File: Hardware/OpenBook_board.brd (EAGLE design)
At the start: 174.6 x 111.2 mm, 103 parts, among them IC1 BD5229G-TR, IC4 XC6220A331MR-G, J1 FH34SRJ-24S-0.5SH_99_, J2 SAMACSYS_PARTS_USB4110-GF-A, J3 QWIIC_RIGHT_ANGLE, J4 112A-TAAR-R03_ATTEND, Q1 20V/4.2A/52mΩ/1.4W, Q2 20V/4.2A/52mΩ/1.4W, Q3 SI1308EDL-T1-GE3, U1 W25Q512JVEIQ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

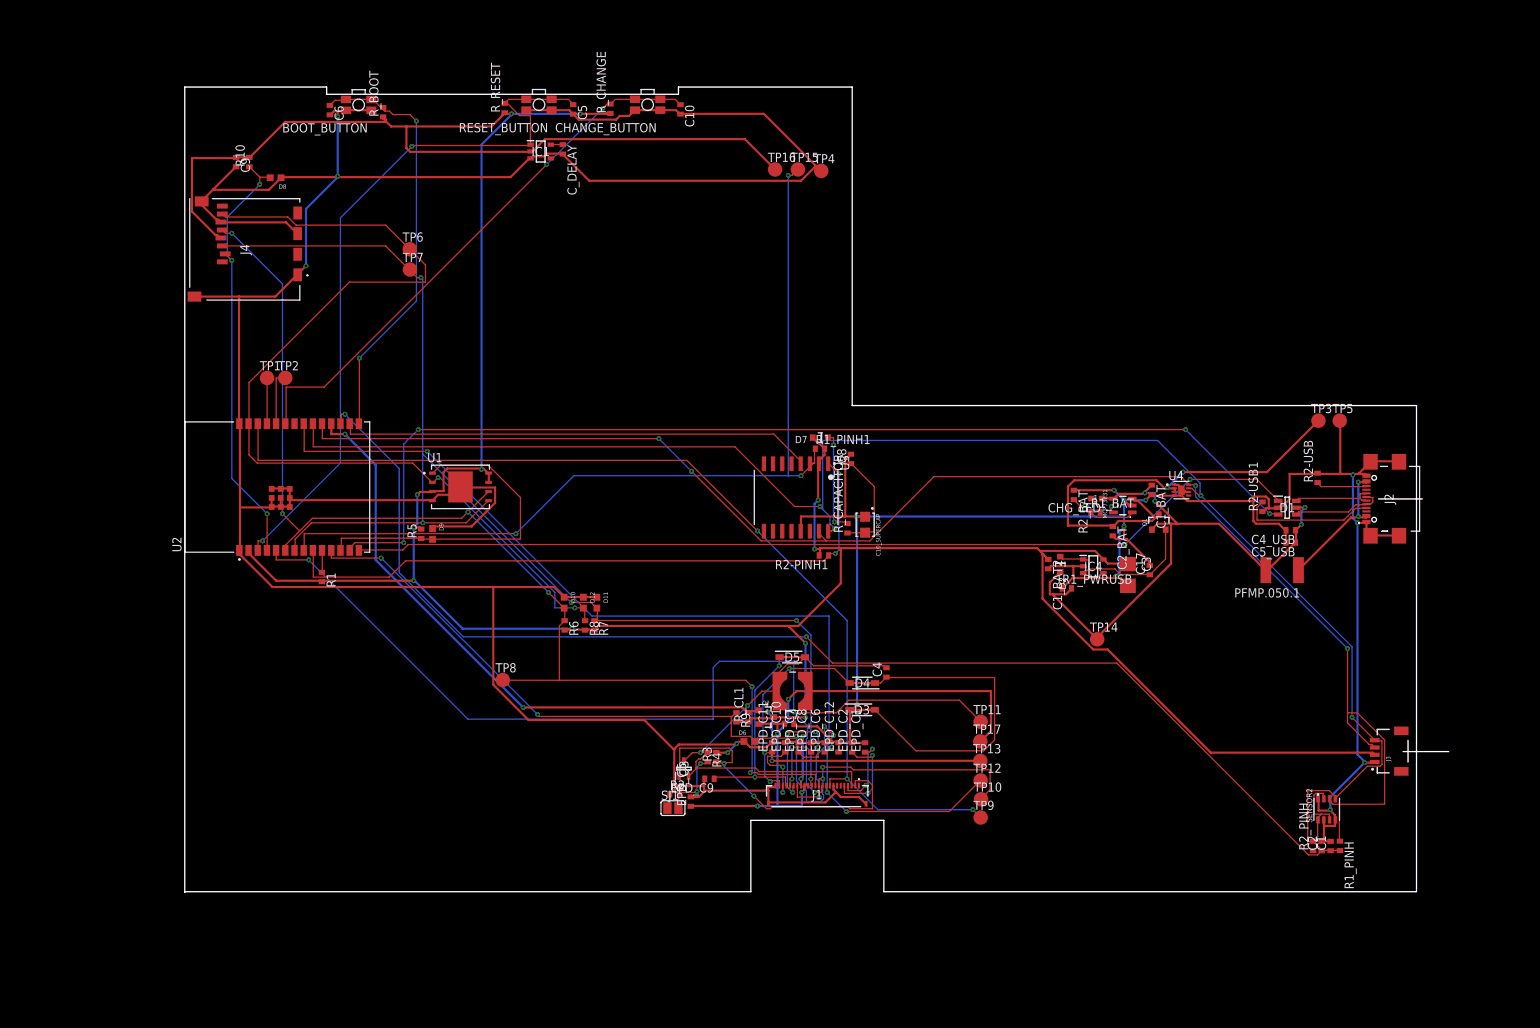
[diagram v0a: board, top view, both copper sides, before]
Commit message: Replaced board and schematic with the correct ones.
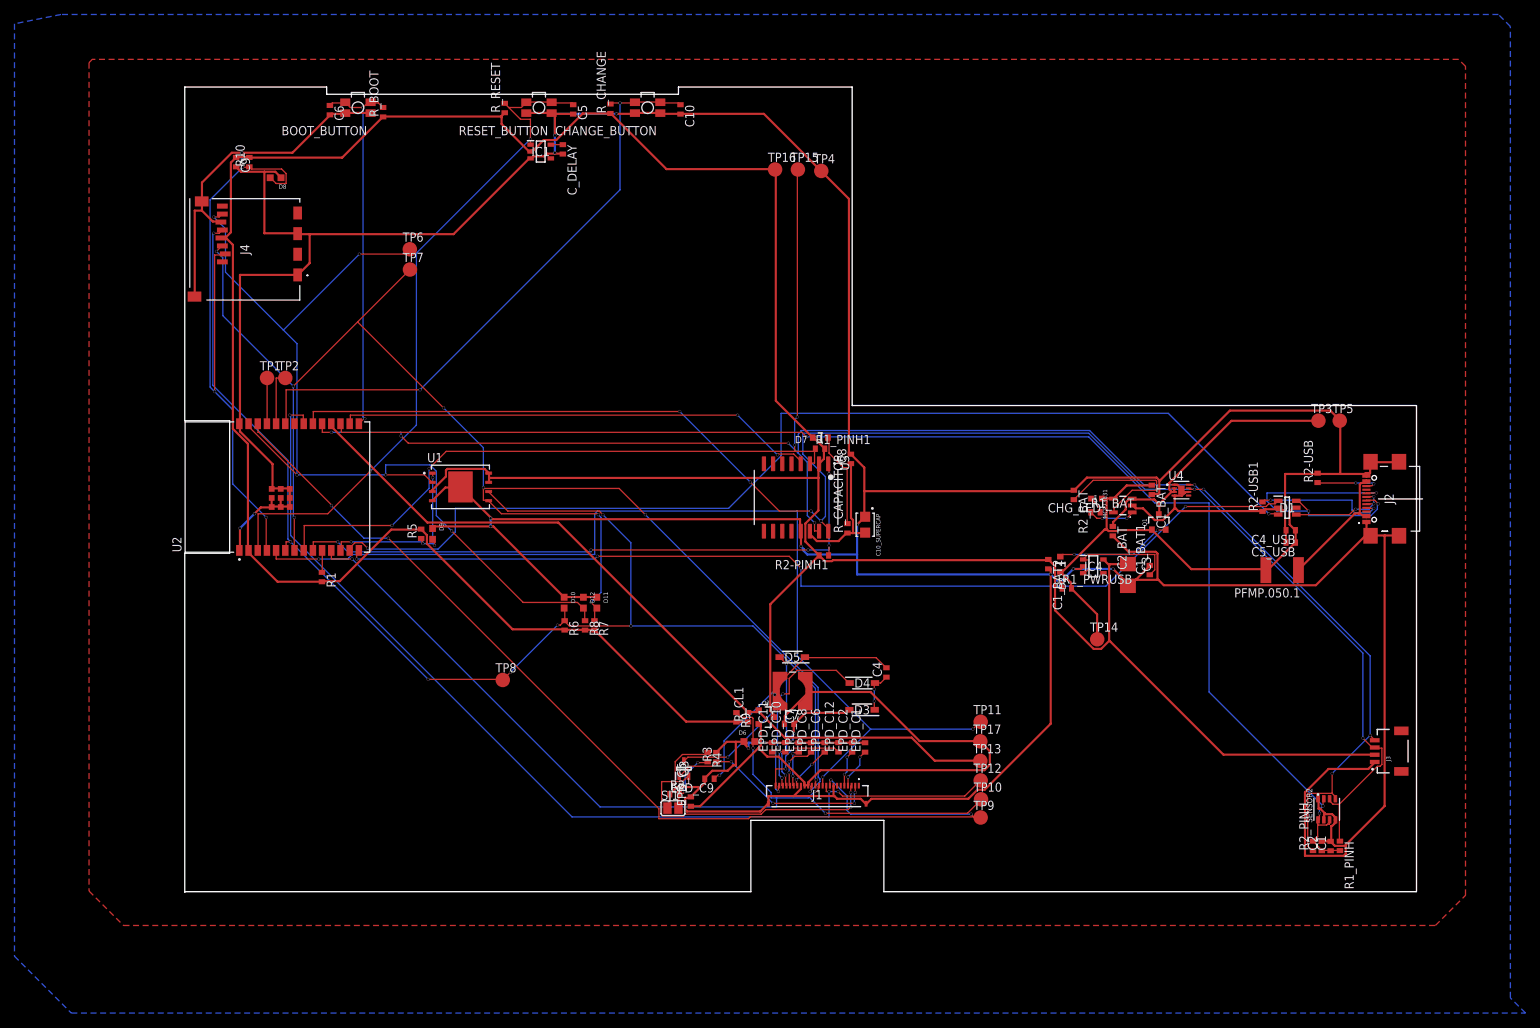
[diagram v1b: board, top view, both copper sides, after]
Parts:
- C1_BAT1, C5_USB: value (none) -> 4.7uF
- C4_USB: value (none) -> 100nF
- R1: value 2K -> 10K
- moved CHANGE_BUTTON 0.41 mm to (63.9, 108.3)
- moved RESET_BUTTON 0.41 mm to (48.9, 108.3)
- moved BOOT_BUTTON 0.40 mm to (23.9, 108.3)
- turned D3 to 180 degrees
- turned D4 to 0 degrees
- turned D5 to 180 degrees
- renumbered C17 to C1_BAT1
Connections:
- removed net N$17: C10_SUPERCAP.2, C8.1, R_CAPACITOR.1
- new net N$2: EPD_C12.1, J1.24
- net GND: no longer EPD_C12.1, J1.24
- net VRTC: now also C10_SUPERCAP.2, C8.1, R_CAPACITOR.1
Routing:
- net GND: track 760.1 -> 843.9 mm, vias 18 -> 19
- net N$7: track 52.0 -> 5.67 mm, vias 0 -> 2
- net SS_SD: track 60.5 -> 88.8 mm
- net DP: track 11.4 -> 39.5 mm, vias 0 -> 3
- net MOSI: track 180.4 -> 207.9 mm, vias 5 -> 9
- net VBAT: track 63.8 -> 39.5 mm, vias 2 -> 0
- net SCK: track 165.0 -> 187.6 mm, vias 6 -> 8
- net FLASH_CS: track 46.8 -> 26.4 mm, vias 0 -> 4
- net 3V3: track 455.6 -> 475.5 mm, vias 11 -> 0
- net VRTC: track 0.00 -> 18.7 mm
- net RESE: track 28.3 -> 46.1 mm, vias 0 -> 2
- net GDR: track 45.5 -> 29.9 mm, vias 2 -> 4
- net N$13: track 20.1 -> 5.40 mm, vias 4 -> 2
- net N$17: track 14.6 -> 0.00 mm
- net N$9: track 7.36 -> 21.4 mm, vias 2 -> 0
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- added copper zone on layer 1, net GND
- added copper zone on layer 16, net GND
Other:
- board size 174.6 x 111.2 mm -> 171 x 111.2 mm
